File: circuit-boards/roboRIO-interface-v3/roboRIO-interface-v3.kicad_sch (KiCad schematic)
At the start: 91 parts, among them J1 DIO0, J10 DIO9, J11 DIO22, J12 DIO23, J13 DIO24, J14 DIO25, J15 RR_DIO0, J16 RR_DIO1, J17 RR_DIO2, J18 RR_DIO3, J19 RR_DIO4, J2 DIO1, J20 RR_DIO5, J21 RR_DIO6, J22 RR_DIO7, J23 RR_DIO8, J24 RR_DIO9, J25 ENC0, J26 ENC1, J27 ENC2, J28 ENC3, J29 ENC4, J3 DIO2, J30 ENC5, J31 ENC_AD0, J32 ENC_AD1, J33 ENC_AD2, J34 ENC_AD3, J35 ENC_AD4, J36 ENC_AD5, J37 RLY0, J38 RLY1, J39 RLY2, J4 DIO3, J40 RLY3, J41 AIN0, J42 AIN1, J43 AIN2, J44 AIN3, J45 AIN4, J46 AIN5, J47 AIN6, J48 AIN7, J49 RR_RELAY0, J5 DIO4, J50 RR_RELAY1, J51 RR_RELAY2, J52 RR_RELAY3, J53 RR_AIN0, J54 RR_AIN1, J55 RR_AIN2, J56 RR_AIN3, J57 PWM0, J58 PWM1, J59 PWM2, J6 DIO5, J60 PWM3, J61 PWM4, J62 PWM5, J63 PWM6, J64 PWM7, J65 PWM8, J66 PWM9, J67 RR_PWM0, J68 RR_PWM1, J69 RR_PWM2, J7 DIO6, J70 RR_PWM3, J71 RR_PWM4, J72 RR_PWM5, J73 RR_PWM6, J74 RR_PWM7, J75 RR_PWM8, J76 RR_PWM9, J77 RSL, J78 RS232, J79 I2C, J8 DIO7, J80 SPI0, J81 SPI1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

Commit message: modify roborio bom to add sockets to bottom of board
Signed-off-by: Scott Berman <sgberman1@gmail.com>
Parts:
- J50, J51, J70, J71, J72, J73, J74, J75: now fitted
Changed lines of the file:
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@@
 		(in_bom yes)
 		(on_board yes)
-		(dnp yes)
+		(dnp no)
 		(fields_autoplaced yes)
 		(property "Reference" "J75"
@@
 		(at 454.66 285.75 0)
 		(unit 1)
-		(exclude_from_sim no)
+		(exclude_from_sim yes)
 		(in_bom no)
 		(on_board yes)
@@
 			)
 		)
-		(property "Sim.Enable" "0"
-			(at 454.66 285.75 0)
-			(effects
-				(font
-					(size 1.27 1.27)
-				)
-				(hide yes)
-			)
-		)
 		(instances
 			(project ""
@@
 		(in_bom yes)
 		(on_board yes)
-		(dnp yes)
+		(dnp no)
 		(fields_autoplaced yes)
 		(property "Reference" "J73"
@@
 		(in_bom yes)
 		(on_board yes)
-		(dnp yes)
+		(dnp no)
 		(fields_autoplaced yes)
 		(property "Reference" "J71"
@@
 		(in_bom yes)
 		(on_board yes)
-		(dnp yes)
+		(dnp no)
 		(fields_autoplaced yes)
 		(property "Reference" "J50"
@@
 		(in_bom yes)
 		(on_board yes)
-		(dnp yes)
+		(dnp no)
 		(fields_autoplaced yes)
 		(property "Reference" "J72"
@@
 		(in_bom yes)
 		(on_board yes)
-		(dnp yes)
+		(dnp no)
 		(fields_autoplaced yes)
 		(property "Reference" "J51"
@@
 		(in_bom yes)
 		(on_board yes)
-		(dnp yes)
+		(dnp no)
 		(fields_autoplaced yes)
 		(property "Reference" "J70"
@@
 		(in_bom yes)
 		(on_board yes)
-		(dnp yes)
+		(dnp no)
 		(fields_autoplaced yes)
 		(property "Reference" "J74"

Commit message: Update RRIB bom to include applicable interfaces
Signed-off-by: Scott Berman <sgberman1@gmail.com>
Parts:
- H1, H2: now left out of the parts list
- J1, J2, J3, J4, J41, J42, J43: now fitted
- J10, J11, J12, J13, J14, J21, J22, J23, J31, J32, J33, J49, J50, J51, J52, J56, J7, J70, J71, J72, J73, J74, J75, J8, J87, J9: now not fitted
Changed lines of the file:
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@@
 	(title_block
 		(title "roboRIO Inteface")
-		(date "2025-12-31")
+		(date "2026-02-08")
 		(rev "3")
 		(company "1868 Space Cookies")
@@
 		(in_bom yes)
 		(on_board yes)
-		(dnp no)
+		(dnp yes)
 		(fields_autoplaced yes)
 		(property "Reference" "J22"
@@
 		(in_bom yes)
 		(on_board yes)
-		(dnp no)
+		(dnp yes)
 		(fields_autoplaced yes)
 		(property "Reference" "J75"
@@
 		(in_bom yes)
 		(on_board yes)
-		(dnp no)
+		(dnp yes)
 		(fields_autoplaced yes)
 		(property "Reference" "J52"
@@
 		(in_bom yes)
 		(on_board yes)
-		(dnp no)
+		(dnp yes)
 		(fields_autoplaced yes)
 		(property "Reference" "J87"
@@
 		(in_bom yes)
 		(on_board yes)
-		(dnp no)
+		(dnp yes)
 		(fields_autoplaced yes)
 		(property "Reference" "J73"
@@
 		(in_bom yes)
 		(on_board yes)
-		(dnp no)
+		(dnp yes)
 		(fields_autoplaced yes)
 		(property "Reference" "J31"
@@
 		(unit 1)
 		(exclude_from_sim no)
-		(in_bom yes)
+		(in_bom no)
 		(on_board yes)
 		(dnp no)
@@
 		(in_bom yes)
 		(on_board yes)
-		(dnp no)
+		(dnp yes)
 		(fields_autoplaced yes)
 		(property "Reference" "J33"
@@
 		(in_bom yes)
 		(on_board yes)
-		(dnp yes)
+		(dnp no)
 		(fields_autoplaced yes)
 		(property "Reference" "J1"
@@
 		(in_bom yes)
 		(on_board yes)
-		(dnp no)
+		(dnp yes)
 		(fields_autoplaced yes)
 		(property "Reference" "J7"
@@
 		(in_bom yes)
 		(on_board yes)
-		(dnp no)
+		(dnp yes)
 		(fields_autoplaced yes)
 		(property "Reference" "J71"
@@
 		(in_bom yes)
 		(on_board yes)
-		(dnp yes)
+		(dnp no)
 		(fields_autoplaced yes)
 		(property "Reference" "J41"
@@
 		(in_bom yes)
 		(on_board yes)
-		(dnp no)
+		(dnp yes)
 		(fields_autoplaced yes)
 		(property "Reference" "J32"
@@
 		(in_bom yes)
 		(on_board yes)
-		(dnp yes)
+		(dnp no)
 		(fields_autoplaced yes)
 		(property "Reference" "J3"
@@
 		(in_bom yes)
 		(on_board yes)
-		(dnp no)
+		(dnp yes)
 		(fields_autoplaced yes)
 		(property "Reference" "J56"
@@
 		(in_bom yes)
 		(on_board yes)
-		(dnp no)
+		(dnp yes)
 		(fields_autoplaced yes)
 		(property "Reference" "J50"
@@
 		(in_bom yes)
 		(on_board yes)
-		(dnp yes)
+		(dnp no)
 		(fields_autoplaced yes)
 		(property "Reference" "J42"
@@
 		(unit 1)
 		(exclude_from_sim no)
-		(in_bom yes)
+		(in_bom no)
 		(on_board yes)
 		(dnp no)
@@
 		(in_bom yes)
 		(on_board yes)
-		(dnp no)
+		(dnp yes)
 		(fields_autoplaced yes)
 		(property "Reference" "J23"
@@
 		(in_bom yes)
 		(on_board yes)
-		(dnp yes)
+		(dnp no)
 		(fields_autoplaced yes)
 		(property "Reference" "J43"
@@
 		(in_bom yes)
 		(on_board yes)
-		(dnp no)
+		(dnp yes)
 		(fields_autoplaced yes)
 		(property "Reference" "J72"
@@
 		(in_bom yes)
 		(on_board yes)
-		(dnp no)
+		(dnp yes)
 		(fields_autoplaced yes)
 		(property "Reference" "J14"
@@
 		(in_bom yes)
 		(on_board yes)
-		(dnp no)
+		(dnp yes)
 		(fields_autoplaced yes)
 		(property "Reference" "J12"
@@
 		(in_bom yes)
 		(on_board yes)
-		(dnp no)
+		(dnp yes)
 		(fields_autoplaced yes)
 		(property "Reference" "J51"
@@
 		(in_bom yes)
 		(on_board yes)
-		(dnp no)
+		(dnp yes)
 		(fields_autoplaced yes)
 		(property "Reference" "J70"
@@
 		(in_bom yes)
 		(on_board yes)
-		(dnp no)
+		(dnp yes)
 		(fields_autoplaced yes)
 		(property "Reference" "J74"
@@
 		(in_bom yes)
 		(on_board yes)
-		(dnp no)
+		(dnp yes)
 		(fields_autoplaced yes)
 		(property "Reference" "J10"
@@
 		(in_bom yes)
 		(on_board yes)
-		(dnp yes)
+		(dnp no)
 		(fields_autoplaced yes)
 		(property "Reference" "J2"
@@
 		(in_bom yes)
 		(on_board yes)
-		(dnp no)
+		(dnp yes)
 		(fields_autoplaced yes)
 		(property "Reference" "J13"
@@
 		(in_bom yes)
 		(on_board yes)
-		(dnp no)
+		(dnp yes)
 		(fields_autoplaced yes)
 		(property "Reference" "J49"
@@
 		(in_bom yes)
 		(on_board yes)
-		(dnp yes)
+		(dnp no)
 		(fields_autoplaced yes)
 		(property "Reference" "J4"
@@
 		(in_bom yes)
 		(on_board yes)
-		(dnp no)
+		(dnp yes)
 		(fields_autoplaced yes)
 		(property "Reference" "J8"
@@
 		(in_bom yes)
 		(on_board yes)
-		(dnp no)
+		(dnp yes)
 		(fields_autoplaced yes)
 		(property "Reference" "J11"
@@
 		(in_bom yes)
 		(on_board yes)
-		(dnp no)
+		(dnp yes)
 		(fields_autoplaced yes)
 		(property "Reference" "J9"
@@
 		(in_bom yes)
 		(on_board yes)
-		(dnp no)
+		(dnp yes)
 		(fields_autoplaced yes)
 		(property "Reference" "J21"

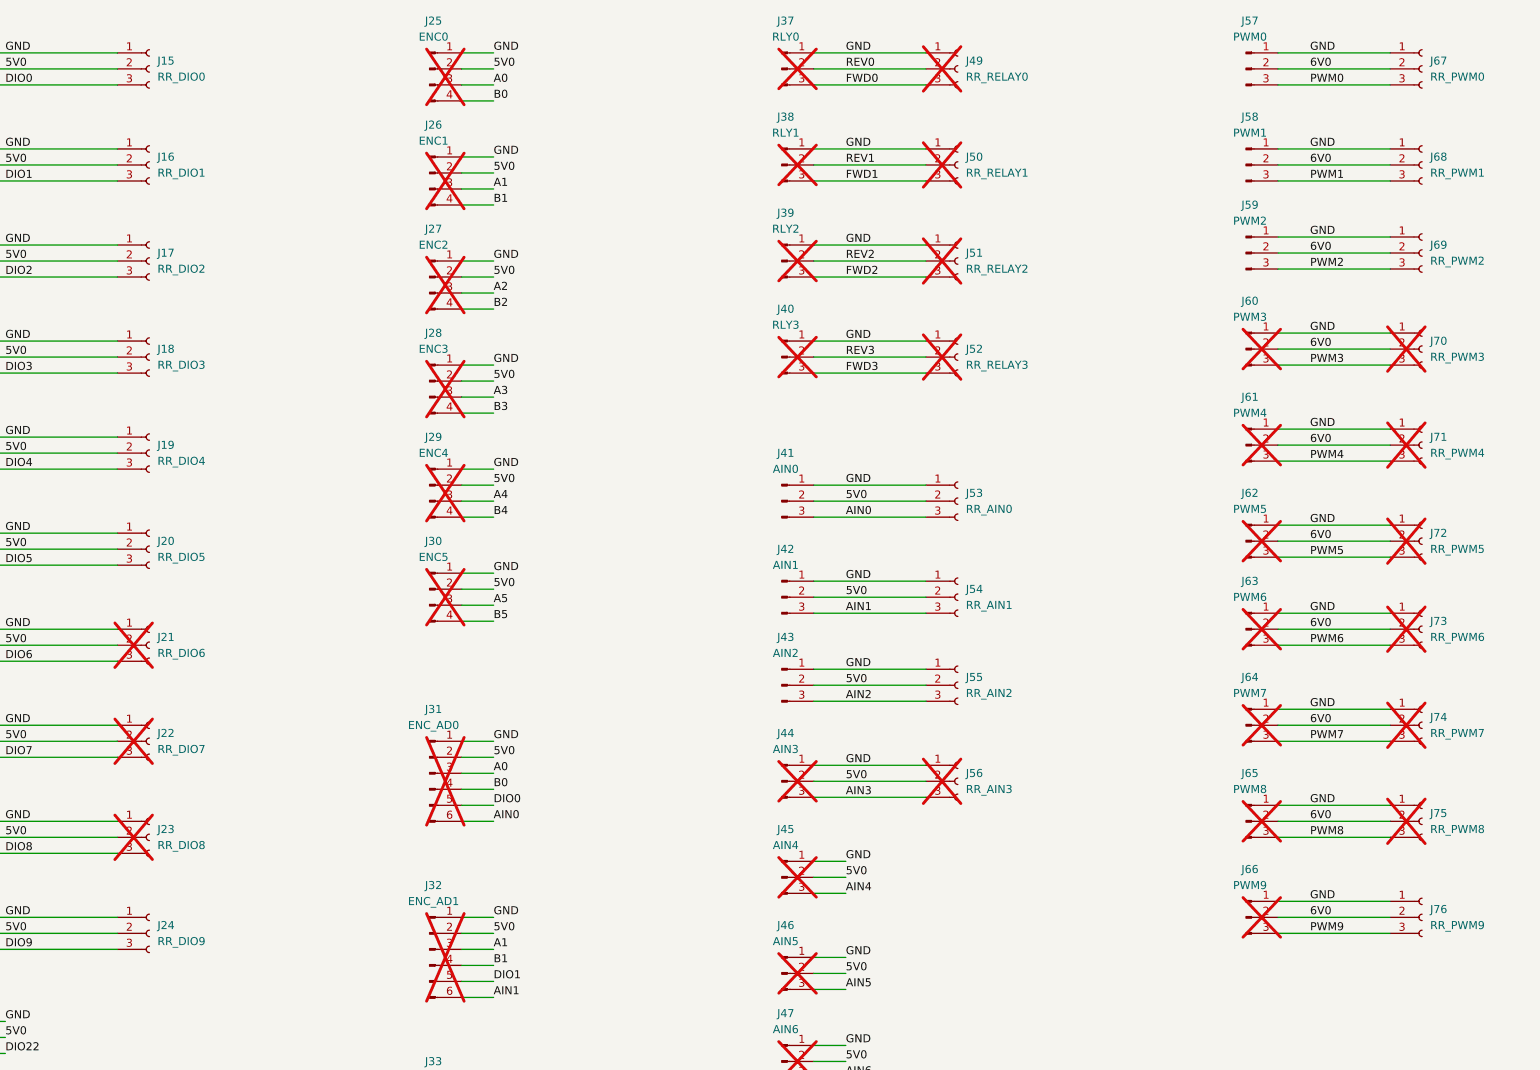
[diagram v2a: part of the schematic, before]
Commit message: changed the roborio interface stuffing
Signed-off-by: Scott Berman <sgberman1@gmail.com>
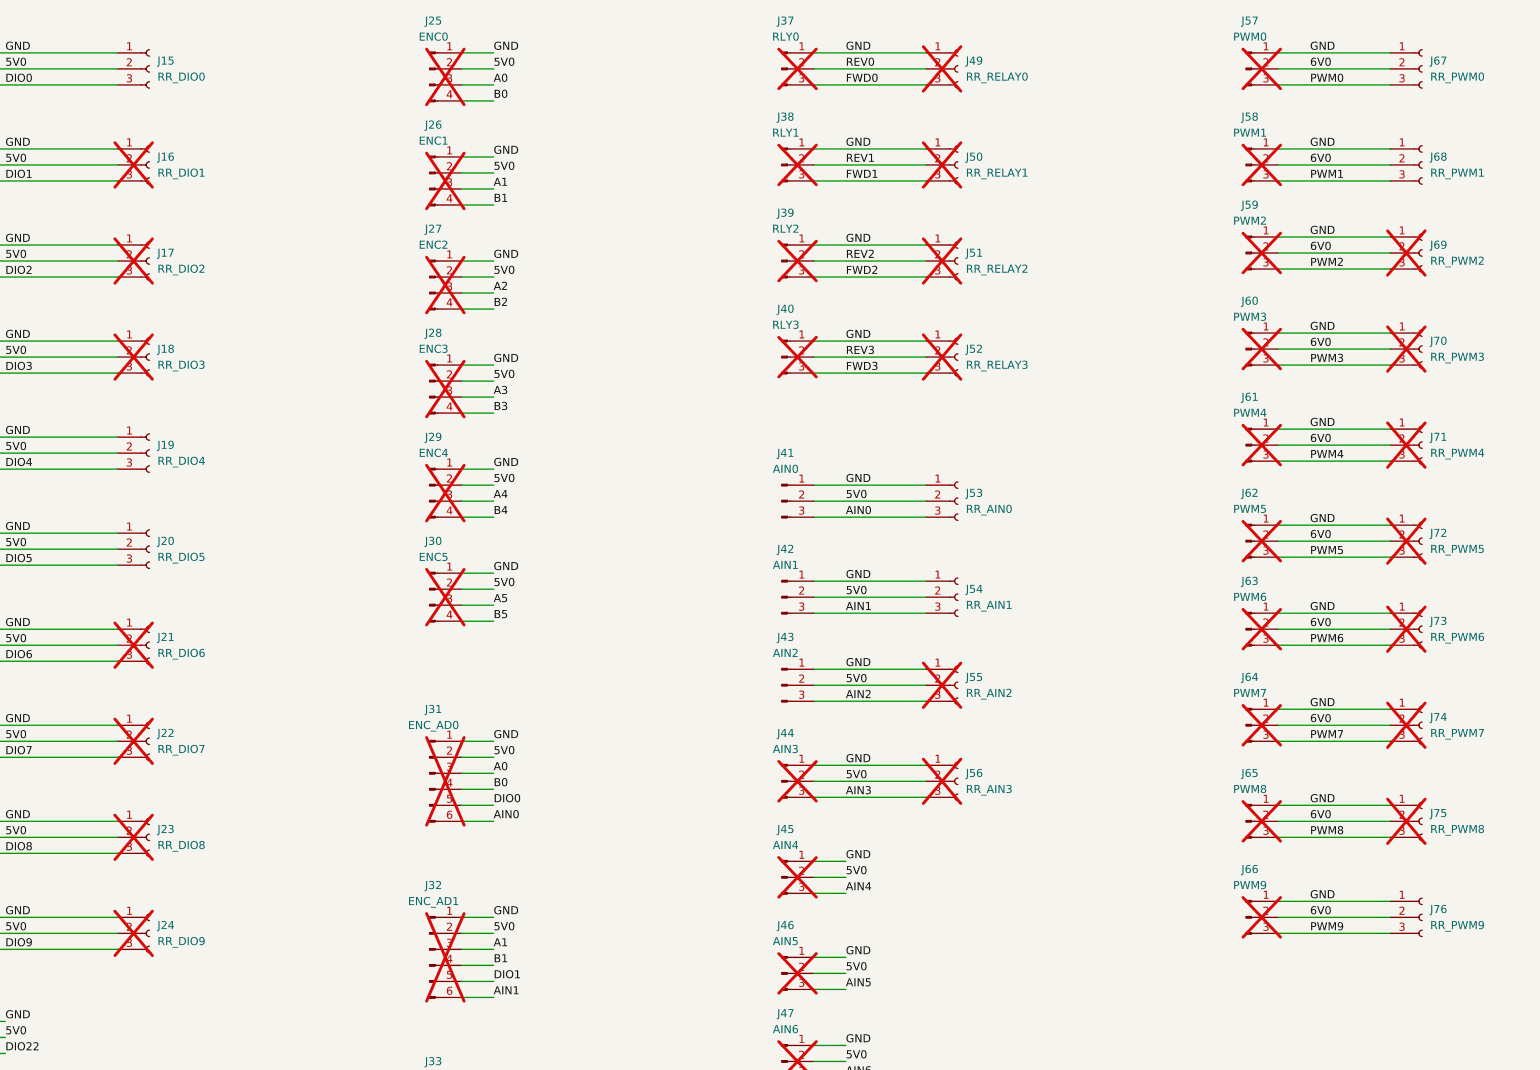
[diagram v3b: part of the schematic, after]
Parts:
- J16, J17, J18, J24, J55, J57, J58, J59, J69: now not fitted
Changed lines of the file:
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@@
 		(in_bom yes)
 		(on_board yes)
-		(dnp no)
+		(dnp yes)
 		(fields_autoplaced yes)
 		(property "Reference" "J24"
@@
 		(in_bom yes)
 		(on_board yes)
-		(dnp no)
+		(dnp yes)
 		(fields_autoplaced yes)
 		(property "Reference" "J59"
@@
 		(in_bom yes)
 		(on_board yes)
-		(dnp no)
+		(dnp yes)
 		(fields_autoplaced yes)
 		(property "Reference" "J18"
@@
 		(in_bom yes)
 		(on_board yes)
-		(dnp no)
+		(dnp yes)
 		(fields_autoplaced yes)
 		(property "Reference" "J16"
@@
 		(in_bom yes)
 		(on_board yes)
-		(dnp no)
+		(dnp yes)
 		(fields_autoplaced yes)
 		(property "Reference" "J17"
@@
 		(in_bom yes)
 		(on_board yes)
-		(dnp no)
+		(dnp yes)
 		(fields_autoplaced yes)
 		(property "Reference" "J58"
@@
 		(in_bom yes)
 		(on_board yes)
-		(dnp no)
+		(dnp yes)
 		(fields_autoplaced yes)
 		(property "Reference" "J55"
@@
 		(in_bom yes)
 		(on_board yes)
-		(dnp no)
+		(dnp yes)
 		(fields_autoplaced yes)
 		(property "Reference" "J57"
@@
 		(in_bom yes)
 		(on_board yes)
-		(dnp no)
+		(dnp yes)
 		(fields_autoplaced yes)
 		(property "Reference" "J69"

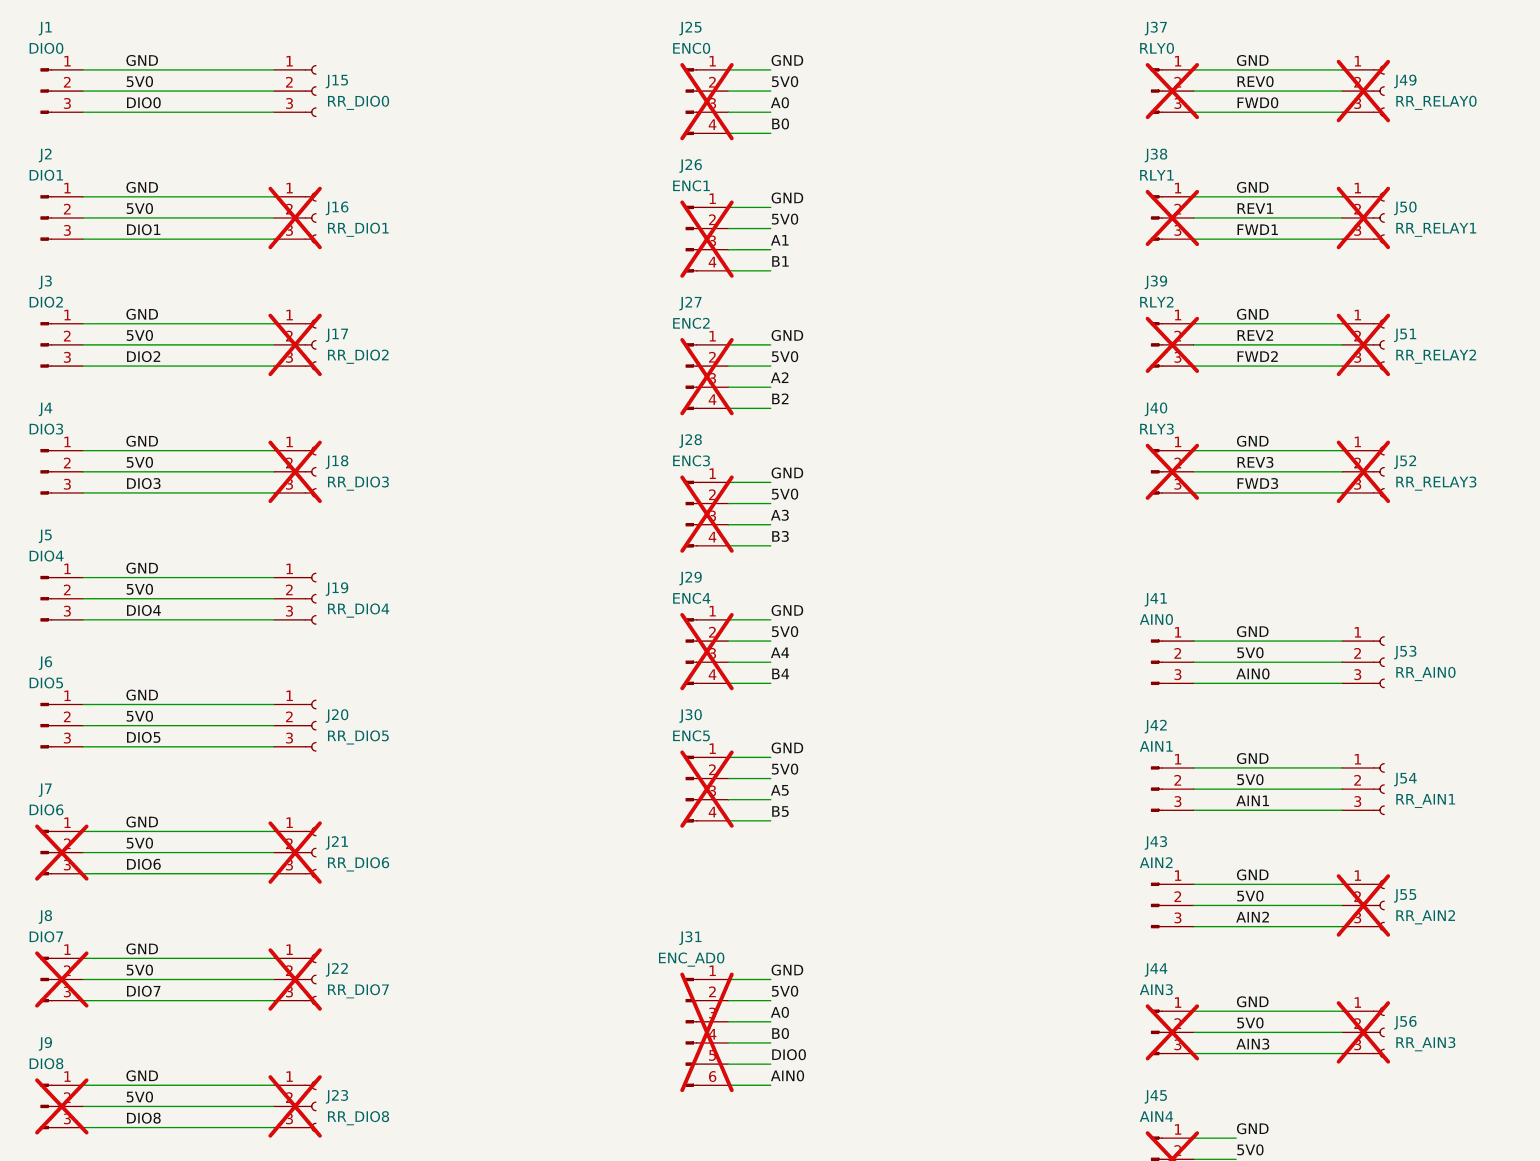
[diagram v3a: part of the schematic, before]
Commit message: Update roborio interface assy
Signed-off-by: Scott Berman <sgberman1@gmail.com>
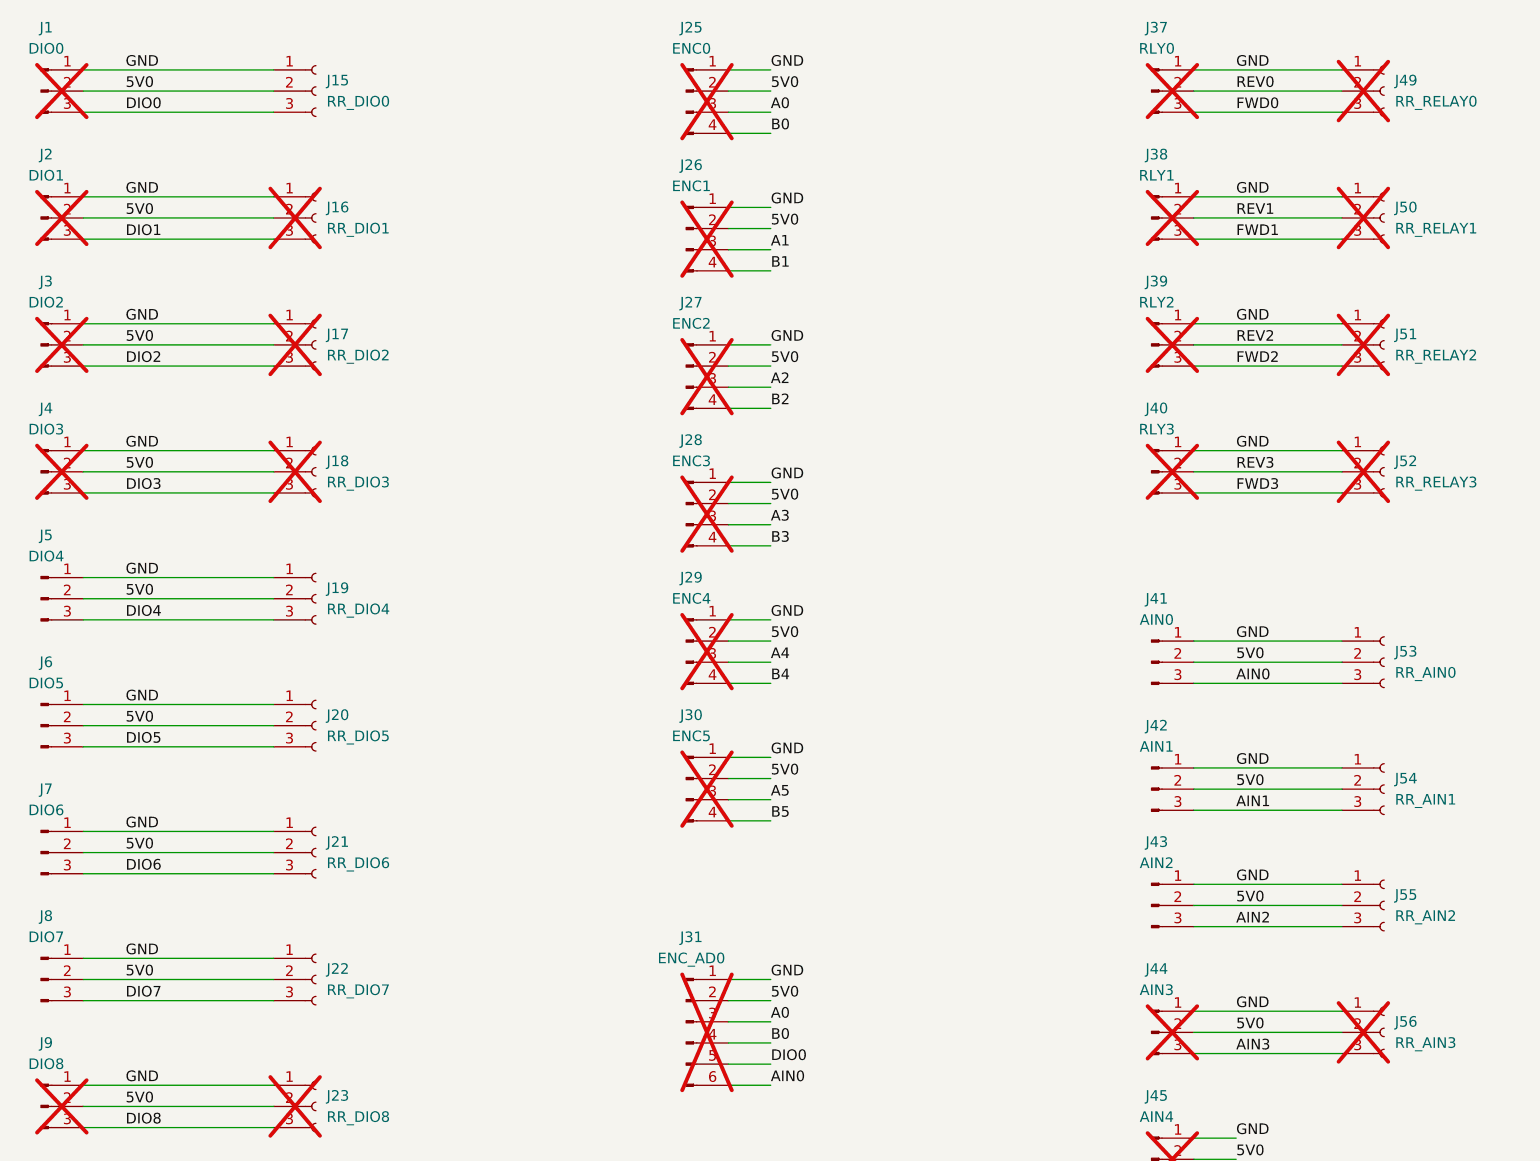
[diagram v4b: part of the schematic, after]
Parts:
- J1, J2, J3, J4: now not fitted
- J21, J22, J55, J7, J8: now fitted
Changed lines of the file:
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@@
 		(in_bom yes)
 		(on_board yes)
-		(dnp yes)
+		(dnp no)
 		(fields_autoplaced yes)
 		(property "Reference" "J22"
@@
 		(in_bom yes)
 		(on_board yes)
-		(dnp no)
+		(dnp yes)
 		(fields_autoplaced yes)
 		(property "Reference" "J1"
@@
 		(in_bom yes)
 		(on_board yes)
-		(dnp yes)
+		(dnp no)
 		(fields_autoplaced yes)
 		(property "Reference" "J7"
@@
 		(in_bom yes)
 		(on_board yes)
-		(dnp no)
+		(dnp yes)
 		(fields_autoplaced yes)
 		(property "Reference" "J3"
@@
 		(in_bom yes)
 		(on_board yes)
-		(dnp yes)
+		(dnp no)
 		(fields_autoplaced yes)
 		(property "Reference" "J55"
@@
 		(in_bom yes)
 		(on_board yes)
-		(dnp no)
+		(dnp yes)
 		(fields_autoplaced yes)
 		(property "Reference" "J2"
@@
 		(in_bom yes)
 		(on_board yes)
-		(dnp no)
+		(dnp yes)
 		(fields_autoplaced yes)
 		(property "Reference" "J4"
@@
 		(in_bom yes)
 		(on_board yes)
-		(dnp yes)
+		(dnp no)
 		(fields_autoplaced yes)
 		(property "Reference" "J8"
@@
 		(in_bom yes)
 		(on_board yes)
-		(dnp yes)
+		(dnp no)
 		(fields_autoplaced yes)
 		(property "Reference" "J21"
